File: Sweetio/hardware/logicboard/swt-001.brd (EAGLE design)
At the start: 91 x 90 mm, 49 parts, among them IC1 74ACT06N, J1 MKR, J10 THS, J16 MNTR, J2 GPIO, J20 GPIO, J21 Grove, J22 Grove, J23 Grove, J24 Grove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

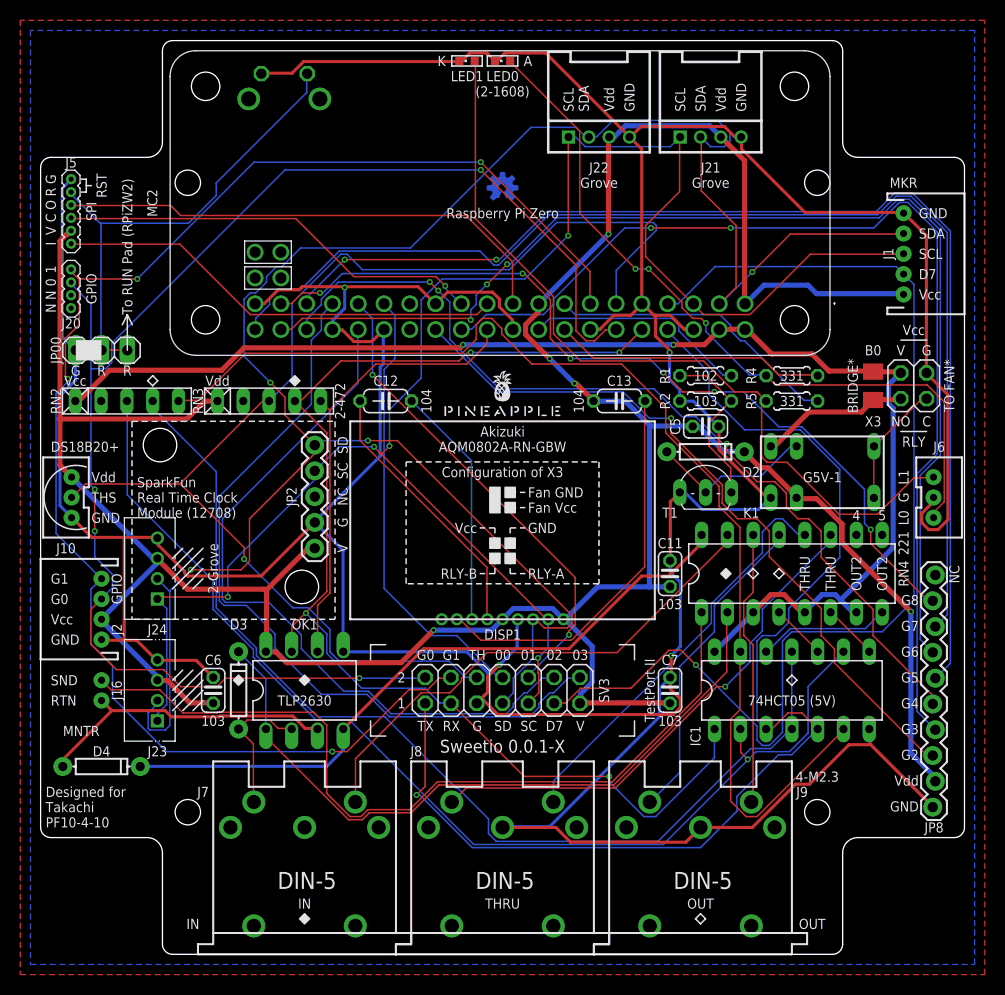
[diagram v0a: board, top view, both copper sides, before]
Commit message: Fixed signaling.
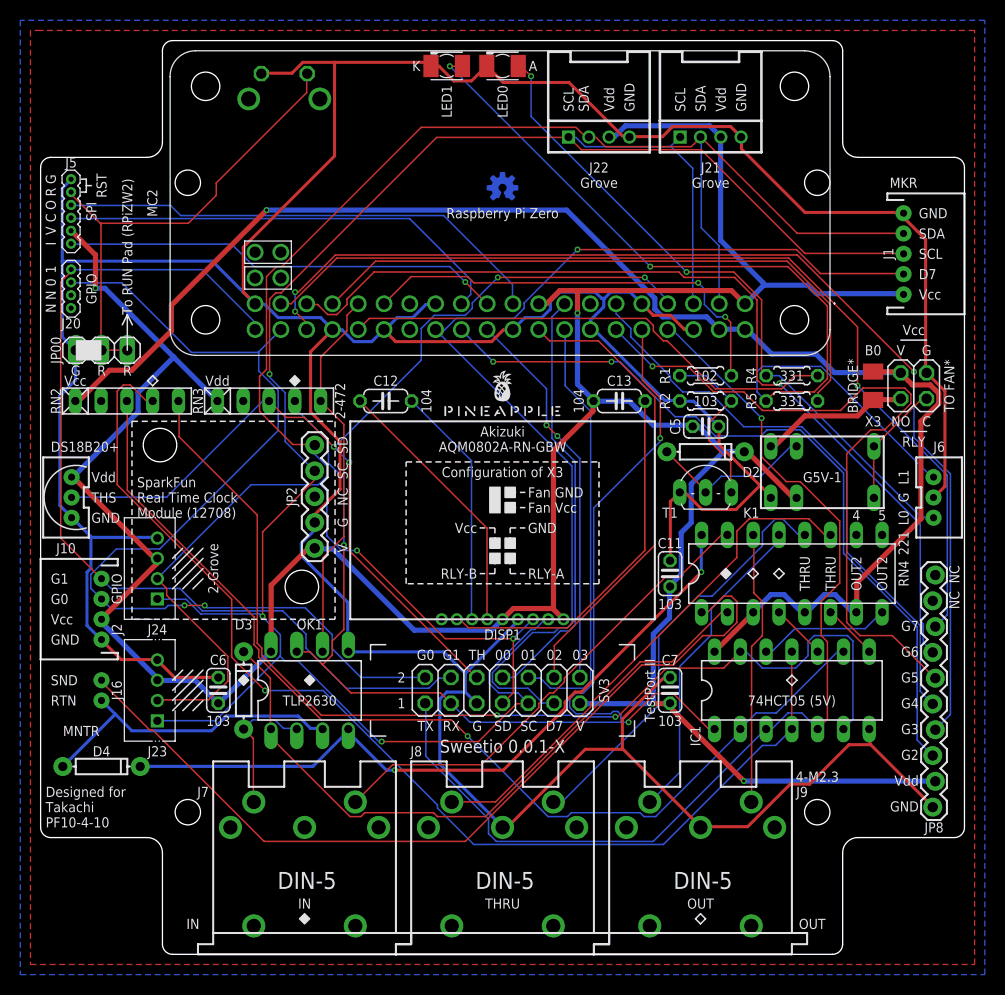
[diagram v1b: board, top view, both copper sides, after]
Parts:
- LED0, LED1: device led:CHIPLED_0603 -> led:KA-3528ASYC
- moved LED1 2.06 mm to (40.0, 87.5), turned to 180 degrees
- moved C6 0.50 mm to (17.5, 26.0)
- moved D3 0.50 mm to (20.0, 26.0)
- moved LED0 0.50 mm to (45.5, 87.5), turned to 180 degrees
- moved OK1 0.50 mm to (26.5, 26.0)
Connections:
- removed net GPIO8: JP8.9, MC2.37
- net DIGITAL7: now also MC2.26; no longer MC2.7
- net DTCT0: now also MC2.15; no longer MC2.29
- net DTCT1: now also MC2.16; no longer MC2.31
- net DTCT2: now also MC2.18; no longer MC2.32
- net DTCT3: now also MC2.22; no longer MC2.33
- net GPIO0: now also MC2.38; no longer MC2.12
- net GPIO1: now also MC2.40; no longer MC2.13
- net GPIO2: now also MC2.24; no longer MC2.26
- net GPIO3: now also MC2.36; no longer MC2.24
- net GPIO4: now also MC2.11; no longer MC2.36
- net GPIO5: now also MC2.12; no longer MC2.35
- net GPIO6: now also MC2.35; no longer MC2.38
- net GPIO7: now also MC2.37; no longer MC2.40
- net LED0: now also MC2.32; no longer MC2.16
- net LED1: now also MC2.33; no longer MC2.15
- net MNTR: now also MC2.31; no longer MC2.22
- net RLY: now also MC2.29; no longer MC2.18
- net THS: now also MC2.7; no longer MC2.11
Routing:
- net GPIO8: track 83.8 -> 0.00 mm, vias 6 -> 0
- net GPIO1: track 148.2 -> 93.7 mm, vias 4 -> 0
- net GPIO0: track 145.5 -> 96.3 mm, vias 4 -> 2
- net GPIO5: track 114.5 -> 70.4 mm, vias 2 -> 1
- net DTCT3: track 76.8 -> 38.1 mm, vias 0 -> 2
- net SCL: track 174.9 -> 211.1 mm, vias 5 -> 3
- net LED1: track 29.2 -> 62.6 mm
- net GPIO4: track 88.6 -> 57.2 mm, vias 3 -> 0
- net DTCT2: track 71.9 -> 45.9 mm
- net GPIO6: track 115.7 -> 91.1 mm, vias 3 -> 1
- net LED0: track 26.8 -> 49.4 mm
- net GPIO7: track 116.5 -> 95.1 mm, vias 0 -> 1
- net RLY: track 22.1 -> 43.3 mm, vias 0 -> 2
- net THS: track 123.0 -> 103.4 mm, vias 1 -> 4
- net VCC: track 129.9 -> 148.7 mm, vias 2 -> 1
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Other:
- board text removed: "(2-1608)"

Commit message: Fixed Sweetio.
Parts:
- moved LOGO1 2.00 mm to (45.5, 73.5)
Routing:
- net SDA: track 194.3 -> 259.0 mm, vias 2 -> 4
- net SCL: track 211.1 -> 238.5 mm
- net LED0A: track 65.8 -> 90.1 mm, vias 2 -> 1
- net NMO2RTN: track 103.9 -> 123.2 mm, vias 2 -> 1
- net DTCT3: track 38.1 -> 56.1 mm, vias 2 -> 1
- net GPIO5: track 70.4 -> 52.8 mm, vias 1 -> 2
- net VDD: track 313.8 -> 330.9 mm
- net RX: track 124.0 -> 140.7 mm, vias 3 -> 1
- net GPIO7: track 95.1 -> 110.2 mm, vias 1 -> 2
- net DIGITAL7: track 103.2 -> 117.3 mm, vias 1 -> 2
- net GND: track 466.8 -> 479.7 mm, vias 0 -> 3
- net GPIO6: track 91.1 -> 100.3 mm, vias 1 -> 2
- net NMORTN: track 110.6 -> 102.3 mm
- net MIDIINSND: track 66.4 -> 74.4 mm
- net MNTRA: track 84.6 -> 76.8 mm, vias 0 -> 2
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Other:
- board text removed: "G8"
